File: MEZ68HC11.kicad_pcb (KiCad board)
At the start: 2 copper layers, 99.1 x 85.2 mm, 29 parts, among them J1 Conn_01x20_Socket, J2 Conn_01x20_Socket, J3 Barrel_Jack_Switch, J4 Conn_01x06_Pin, J5 Conn_01x08_Pin, J7 PinHeader_1x06_P2.54mm_Vertic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, SW1 SW_SPDT, SW2 SW_SPST, U1 PIC18F47Q43-IP, U2 628128

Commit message: Rev001. ordered to JCLPCB
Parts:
- removed D1: 1N4148, Diode_THT:D_DO-35_SOD27_P7.62mm_Horizontal
- removed D2: LED, LED_THT:LED_D3.0mm
- removed DIP40-48 CPU: DIP-48_W15.24mm_Socket_OvalPad_nocourtyard, 0-local:DIP-48_W15.24mm_Socket_OvalPad_splitcouryard
- removed H5, H6: MountingHole, MountingHole:MountingHole_3.5mm
- removed J7: PinHeader_1x06_P2.54mm_Vertical, Connector_PinHeader_2.54mm:PinHeader_1x06_P2.54mm_Vertical
- removed R3: 1.5k, Resistor_THT:R_Axial_DIN0204_L3.6mm_D1.6mm_P7.62mm_Horizontal
- removed R5, R6: 10k, Resistor_THT:R_Axial_DIN0204_L3.6mm_D1.6mm_P7.62mm_Horizontal
- removed SW1: SW_SPDT, 0-local:PowerSW_for_SBC_series
- removed SW2: SW_SPST, 0-local:SW_PUSH_6mm_H4.3mm
- added JP2: SolderJumper_2_Open, Jumper:SolderJumper-2_P1.3mm_Open_RoundedPad1.0x1.5mm, F.Cu at (173.3, 148.6)
- added JP3: SolderJumper_2_Open, Jumper:SolderJumper-2_P1.3mm_Open_RoundedPad1.0x1.5mm, F.Cu at (139.1, 127.0)
- added RN1: 10kx8, Resistor_THT:R_Array_SIP9, F.Cu at (143.5, 98.8)
- added RN2: 10kx8, Resistor_THT:R_Array_SIP9, F.Cu at (119.4, 98.8)
- added RN3: 10kx8, Resistor_THT:R_Array_SIP9, F.Cu at (161.3, 99.1)
- added Y1: 8MHz, Crystal:Crystal_HC49-U_Vertical, F.Cu at (130.9, 133.3)
- C1, C2: footprint Capacitor_THT:C_Disc_D3.0mm_W2.0mm_P2.50mm -> Capacitor_THT:C_Disc_D3.0mm_W1.6mm_P2.50mm
- C3: value 10uF -> 0.1uF; footprint Capacitor_THT:CP_Radial_D5.0mm_P2.50mm -> Capacitor_THT:C_Disc_D3.0mm_W1.6mm_P2.50mm
- C4, C5: value 0.1uF -> 22pF; footprint Capacitor_THT:C_Disc_D3.0mm_W2.0mm_P2.50mm -> Capacitor_THT:C_Disc_D3.0mm_W1.6mm_P2.50mm
- C6: value 0.1uF -> 10uF; footprint Capacitor_THT:C_Disc_D3.0mm_W2.0mm_P2.50mm -> Capacitor_THT:CP_Radial_D4.0mm_P2.00mm
- J3: value Barrel_Jack_Switch -> Conn_01x08_Socket; footprint 0-local:BARREL_JACK -> Connector_PinSocket_2.54mm:PinSocket_1x08_P2.54mm_Vertical
- J4: value Conn_01x06_Pin -> Conn_01x08_Socket; footprint 0-local:PinHeader_1x06_P2.54mm_Horizontal_NoFeet -> Connector_PinSocket_2.54mm:PinSocket_1x08_P2.54mm_Vertical
- J5: value Conn_01x08_Pin -> Conn_01x08_Socket; footprint 0-local:PinHeader_1x08_P2.54mm_Rev_Horizontal_Nofoot -> Connector_PinSocket_2.54mm:PinSocket_1x08_P2.54mm_Vertical
- JP1: value SolderJumper_2_Bridged -> SolderJumper_2_Open; footprint Jumper:SolderJumper-2_P1.3mm_Bridged_RoundedPad1.0x1.5mm -> Jumper:SolderJumper-2_P1.3mm_Open_RoundedPad1.0x1.5mm
- R1: value 10k -> 10M
- R2: value 10k -> 1k
- U1: value PIC18F47Q43-IP -> 68HC11_PLCC; footprint Package_DIP:DIP-40_W15.24mm -> Package_LCC:PLCC-52
- U2: value 628128 -> 74HC573; footprint Package_DIP:DIP-32_W15.24mm_Socket -> Package_DIP:DIP-20_W7.62mm
- moved C2 76.3 mm to (170.1, 95.2), turned to 180 degrees
- moved C3 57.6 mm to (120.7, 130.8), turned to 0 degrees
- moved C5 51.3 mm to (129.5, 141.0), turned to 0 degrees
- moved J3 49.4 mm to (99.1, 90.1), turned to 90 degrees
- moved R1 46.0 mm to (137.2, 138.4), turned to 180 degrees
- moved JP1 41.3 mm to (126.4, 146.1), turned to 180 degrees
- moved R2 40.7 mm to (123.2, 133.3), turned to 180 degrees
- moved C1 40.6 mm to (125.7, 106.4), turned to 180 degrees
- moved J5 39.4 mm to (92.7, 115.6), turned to 0 degrees
- moved U2 37.3 mm to (165.1, 99.1)
- moved U1 34.2 mm to (124.5, 118.1), turned to 180 degrees
- moved C4 33.5 mm to (137.2, 141.0)
- moved C6 28.5 mm to (146.1, 119.9)
- moved J4 21.8 mm to (143.5, 90.2), turned to -90 degrees
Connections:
- C3 pad 1: VCC -> Net-(U1-VRL)
- C3 pad 2: GND -> Net-(U1-VRH)
- C4 pad 1: VCC -> Net-(U1-XTAL)
- C5 pad 1: VCC -> Net-(JP3-A)
- J3 pad 1: Net-(SW1-C) -> /PA0
- J3 pad 2: GND -> /PA1
- J3 pad 3: unconnected-(J3-Pad3) -> /PA2
- J4 pad 1: unconnected-(J4-Pin_1-Pad1) -> VCC
- J4 pad 3: Net-(D1-K) -> Net-(J4-Pin_3)
- J4 pad 4: VCC -> Net-(J4-Pin_4)
- J4 pad 5: unconnected-(J4-Pin_5-Pad5) -> Net-(J4-Pin_5)
- J4 pad 6: GND -> Net-(J4-Pin_6)
- J5 pad 2: VCC -> Net-(J5-Pin_2)
- J5 pad 3: GND -> Net-(J5-Pin_3)
- J5 pad 4: /A7 -> Net-(J5-Pin_4)
- J5 pad 5: /A6 -> Net-(J5-Pin_5)
- J5 pad 6: unconnected-(J5-Pin_6-Pad6) -> Net-(J5-Pin_6)
- J5 pad 7: unconnected-(J5-Pin_7-Pad7) -> Net-(J5-Pin_7)
- J5 pad 8: unconnected-(J5-Pin_8-Pad8) -> Net-(J5-Pin_8)
- JP1 pad 1: /A14 -> Net-(JP1-A)
- JP1 pad 2: Net-(JP1-B) -> /~{M1}
- R1 pad 1: VCC -> Net-(U1-XTAL)
- R1 pad 2: Net-(D1-A) -> Net-(JP3-A)
- R2 pad 1: VCC -> Net-(U1-VRH)
- R2 pad 2: Net-(J5-Pin_1) -> VCC
- U1 pad 1: Net-(J5-Pin_1) -> GND
- U1 pad 10: Net-(JP1-B) -> /D1
- U1 pad 11: VCC -> /D2
- U1 pad 12: GND -> /D3
- U1 pad 13: Net-(D1-A) -> /D4
- U1 pad 14: Net-(J4-Pin_2) -> /D5
- U1 pad 15: /D0 -> /D6
- U1 pad 16: /D1 -> /D7
- U1 pad 17: /D2 -> /~{RESET}
- U1 pad 18: /D3 -> /~{BUSRQ}
- U1 pad 19: /A8 -> /~{INT}
- U1 pad 2: /~{IORQ} -> /~{M1}
- U1 pad 20: /A9 -> Net-(J4-Pin_2)
- U1 pad 21: /A10 -> Net-(J4-Pin_3)
- U1 pad 22: /A11 -> Net-(J4-Pin_4)
- U1 pad 23: /D4 -> Net-(J4-Pin_5)
- U1 pad 24: /D5 -> Net-(J4-Pin_6)
- U1 pad 25: /D6 -> Net-(J4-Pin_7)
- U1 pad 26: /D7 -> VCC
- U1 pad 27: /A12 -> /PA7
- U1 pad 28: /A13 -> Net-(J3-Pin_7)
- U1 pad 29: /~{WAIT} -> Net-(J3-Pin_6)
- U1 pad 3: /~{MREQ} -> /~{WAIT}
- U1 pad 30: /~{RFSH} -> Net-(J3-Pin_5)
- U1 pad 31: GND -> Net-(J3-Pin_4)
- U1 pad 32: VCC -> /PA2
- U1 pad 33: /A0 -> /PA1
- U1 pad 34: /A1 -> /PA0
- U1 pad 35: /A2 -> /A15
- U1 pad 36: /A3 -> /A14
- U1 pad 37: /A4 -> /A13
- U1 pad 38: /A5 -> /A12
- U1 pad 39: /A6 -> /A11
- U1 pad 4: Net-(U1-RA2) -> Net-(U1-AS)
- U1 pad 40: /A7 -> /A10
- U1 pad 5: /CLK -> /~{MREQ}
- U1 pad 6: Net-(U1-RA4) -> /~{RD}
- U1 pad 7: /~{RD} -> Net-(JP3-A)
- U1 pad 8: /~{BUSRQ} -> Net-(U1-XTAL)
- U1 pad 9: /~{RESET} -> /D0
- U2 pad 1: unconnected-(U2-NC-Pad1) -> GND
- U2 pad 10: /A2 -> GND
- U2 pad 11: /A1 -> Net-(U1-AS)
- U2 pad 13: /D0 -> /A1
- U2 pad 14: /D1 -> /A2
- U2 pad 15: /D2 -> /A3
- U2 pad 16: GND -> /A4
- U2 pad 17: /D3 -> /A5
- U2 pad 18: /D4 -> /A6
- U2 pad 19: /D5 -> /A7
- U2 pad 2: VCC -> /D7
- U2 pad 20: /D6 -> VCC
- U2 pad 3: /A14 -> /D6
- U2 pad 4: /A12 -> /D5
- U2 pad 5: /A7 -> /D4
- U2 pad 6: /A6 -> /D3
- U2 pad 7: /A5 -> /D2
- U2 pad 8: /A4 -> /D1
- U2 pad 9: /A3 -> /D0
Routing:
- net Net-(D1-K): track 125.3 -> 0.00 mm
- net GND: track 341.8 -> 220.5 mm, vias 6 -> 8
- net /A6: track 111.2 -> 3.81 mm, vias 1 -> 0
- net /A7: track 110.9 -> 3.81 mm
- net /~{IORQ}: track 106.8 -> 0.00 mm
- net /A5: track 110.4 -> 3.81 mm
- net VCC: track 326.7 -> 224.8 mm, vias 6 -> 5
- net /A2: track 97.4 -> 3.81 mm, vias 1 -> 0
- net Net-(JP2-A): track 0.00 -> 92.7 mm, vias 0 -> 2
- net /A1: track 96.2 -> 3.81 mm, vias 1 -> 0
- net /A4: track 91.2 -> 3.81 mm, vias 1 -> 0
- net /A0: track 89.0 -> 3.81 mm
- net Net-(J4-Pin_2): track 105.9 -> 24.4 mm, vias 1 -> 0
- net /A3: track 82.7 -> 3.81 mm, vias 1 -> 0
- net /~{M1}: track 0.00 -> 74.5 mm, vias 0 -> 1
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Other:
- board size 99.1 x 85.2 mm -> 99.1 x 63.9 mm
- board text added: "74HC573"
- board text added: "MEZ68HC11_board (C) 2023, N. Kumagai"
- board text added: "PA0"
- board text added: "PA1"
- board text added: "PA2"
- board text added: "PA3"
- board text added: "PA4"
- board text added: "PA5"
- board text added: "PA6"
- board text added: "PA7"
- board text added: "PD0"
- board text added: "PD1"
- board text added: "PD2"
- board text added: "PD3"
- board text added: "PD4"
- board text added: "PD5"
- board text added: "PE0"
- board text added: "PE1"
- board text added: "PE2"
- board text added: "PE3"
- board text added: "PE4"
- board text added: "PE5"
- board text added: "PE6"
- board text added: "PE7"
- board text removed: "628128 SRAM"
- board text removed: "DONTC"
- board text removed: "EMUPU_RAM40 (C) 2023, N. Kumagai"
- board text removed: "MPLAB SNAP"
- board text removed: "NC"
- board text removed: "PGC"
- board text removed: "PGD"
- board text removed: "PIC18F47Q43"
- board text removed: "RXD"
- board text removed: "Serial"
- board text removed: "TXD"
- board text removed: "VDD"
- board text removed: "~{MCLR}"

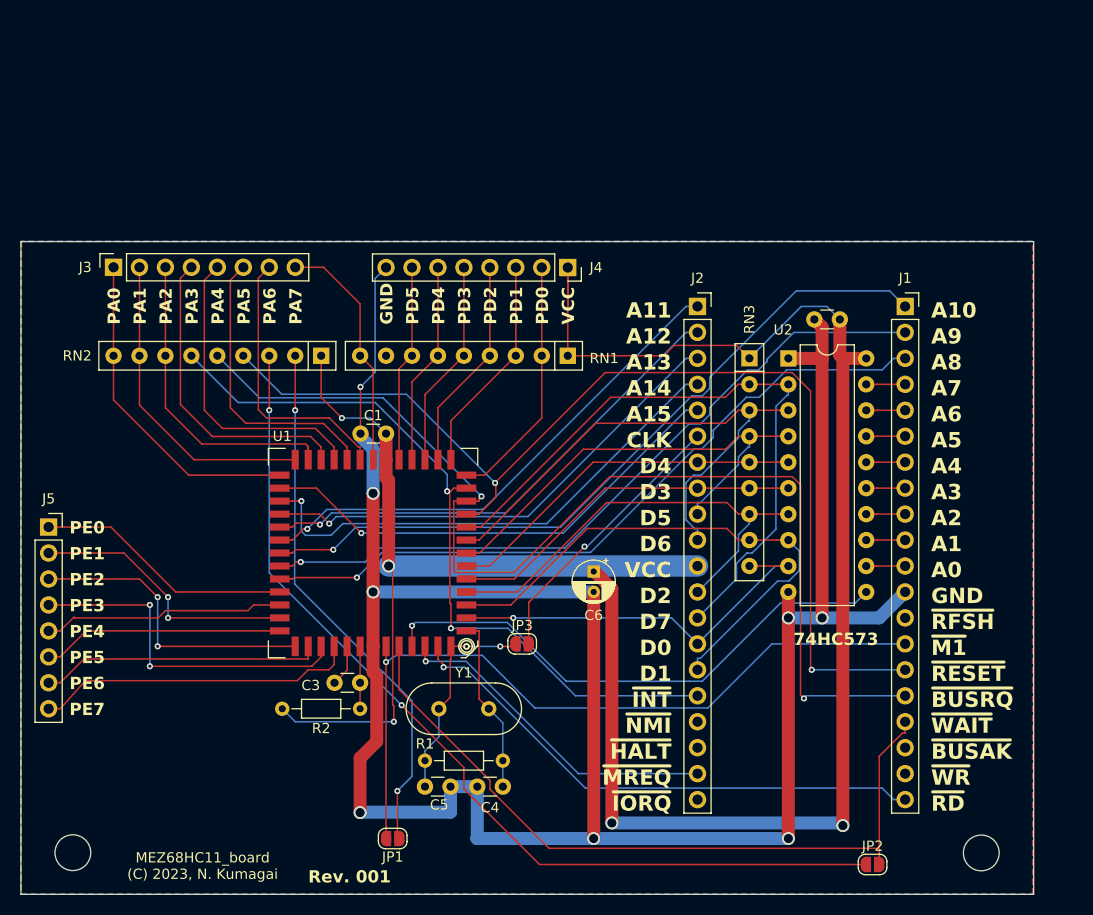
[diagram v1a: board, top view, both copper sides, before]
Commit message: add 4.7k between MODA and PIC
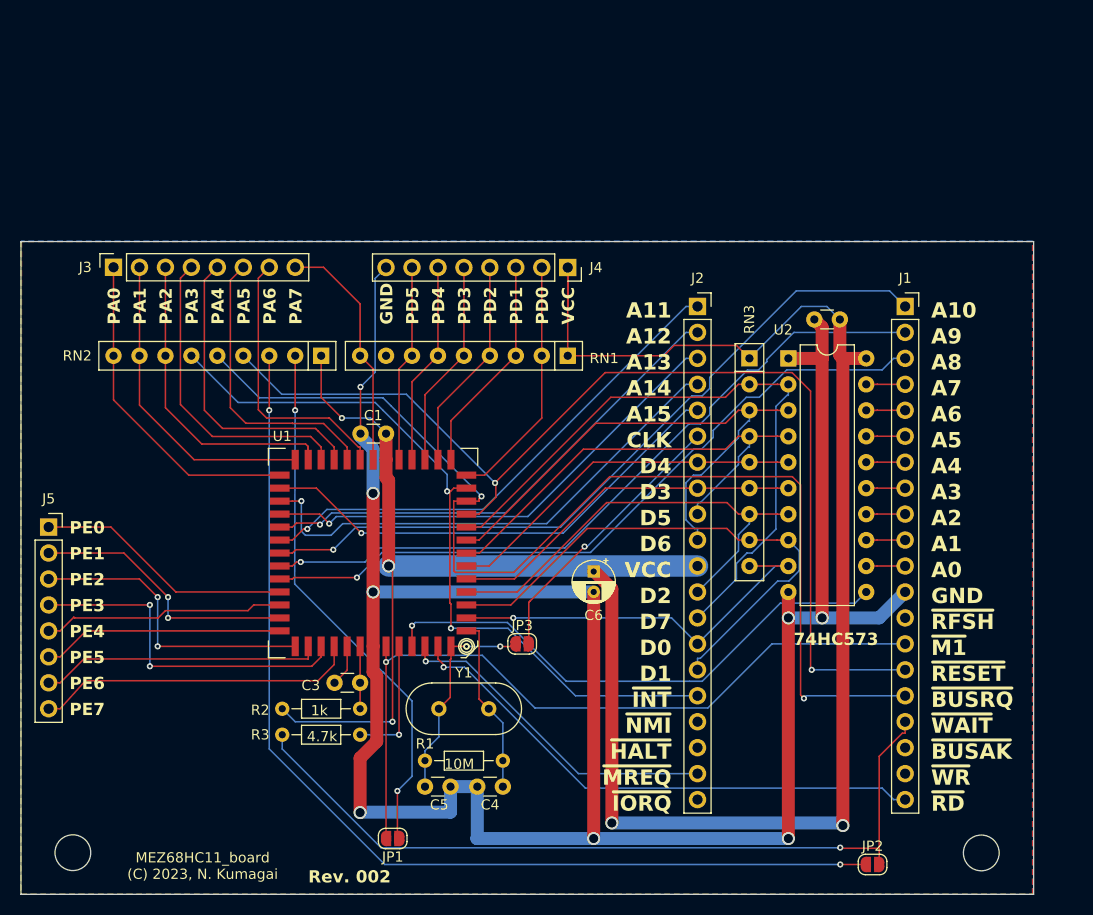
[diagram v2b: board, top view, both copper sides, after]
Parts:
- added R3: 4.7k, Resistor_THT:R_Axial_DIN0204_L3.6mm_D1.6mm_P7.62mm_Horizontal, F.Cu at (115.6, 135.9)
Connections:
- U1 pad 3: /~{WAIT} -> Net-(U1-MODA)
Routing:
- net Net-(U1-MODA): track 0.00 -> 12.5 mm, vias 0 -> 1
- net Net-(JP2-A): track 92.7 -> 101.6 mm
- net /~{WAIT}: track 73.3 -> 79.0 mm, vias 0 -> 1
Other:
- board text added: "10M"
- board text added: "1k"
- board text added: "4.7k"
- board text added: "Rev. 002"
- board text removed: "Rev. 001"
